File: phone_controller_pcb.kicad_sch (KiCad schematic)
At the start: 4 parts, among them U1 nRF52840, Y1 ECS-320-8-37B-CKY-TR, Y2 ABS05-32.768KHZ-9-T

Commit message: Added Usb esd protection
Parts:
- added J1: USB_C_Receptacle_USB2.0_14P, Connector_USB:USB_C_Receptacle_G-Switch_GT-USB-7010ASV, symbol Connector:USB_C_Receptacle_USB2.0_14P
- added U2: USBLC6-2P6, Package_TO_SOT_SMD:SOT-666, symbol Power_Protection:USBLC6-2P6
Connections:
- net GND: now also J1.A1 (GND), J1.A12 (GND), J1.B1 (GND), J1.B12 (GND), J1.S1 (SHIELD)
- net +5V: now reaches U1.AD2 (VBUS)
- net +5V: now also U1.Y2 (VDDH), J1.A4 (VBUS), J1.A9 (VBUS), J1.B4 (VBUS), J1.B9 (VBUS)
- net USB_D-: now reaches U1.AD4 (D-)
- net USB_D-: now also U2.6 (I/O1)
- net USB_D+: now reaches U1.AD6 (D+)
- net USB_D+: now also U2.4 (I/O2)
- new net: J1.A6 (D+), J1.B6 (D+), U2.3 (I/O2)
- new net: J1.A7 (D-), J1.B7 (D-), U2.1 (I/O1)
- new net CC1: J1.A5 (CC1)
- new net CC2: J1.B5 (CC2)
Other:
- moved on the sheet: AE1, U1, Y1, Y2

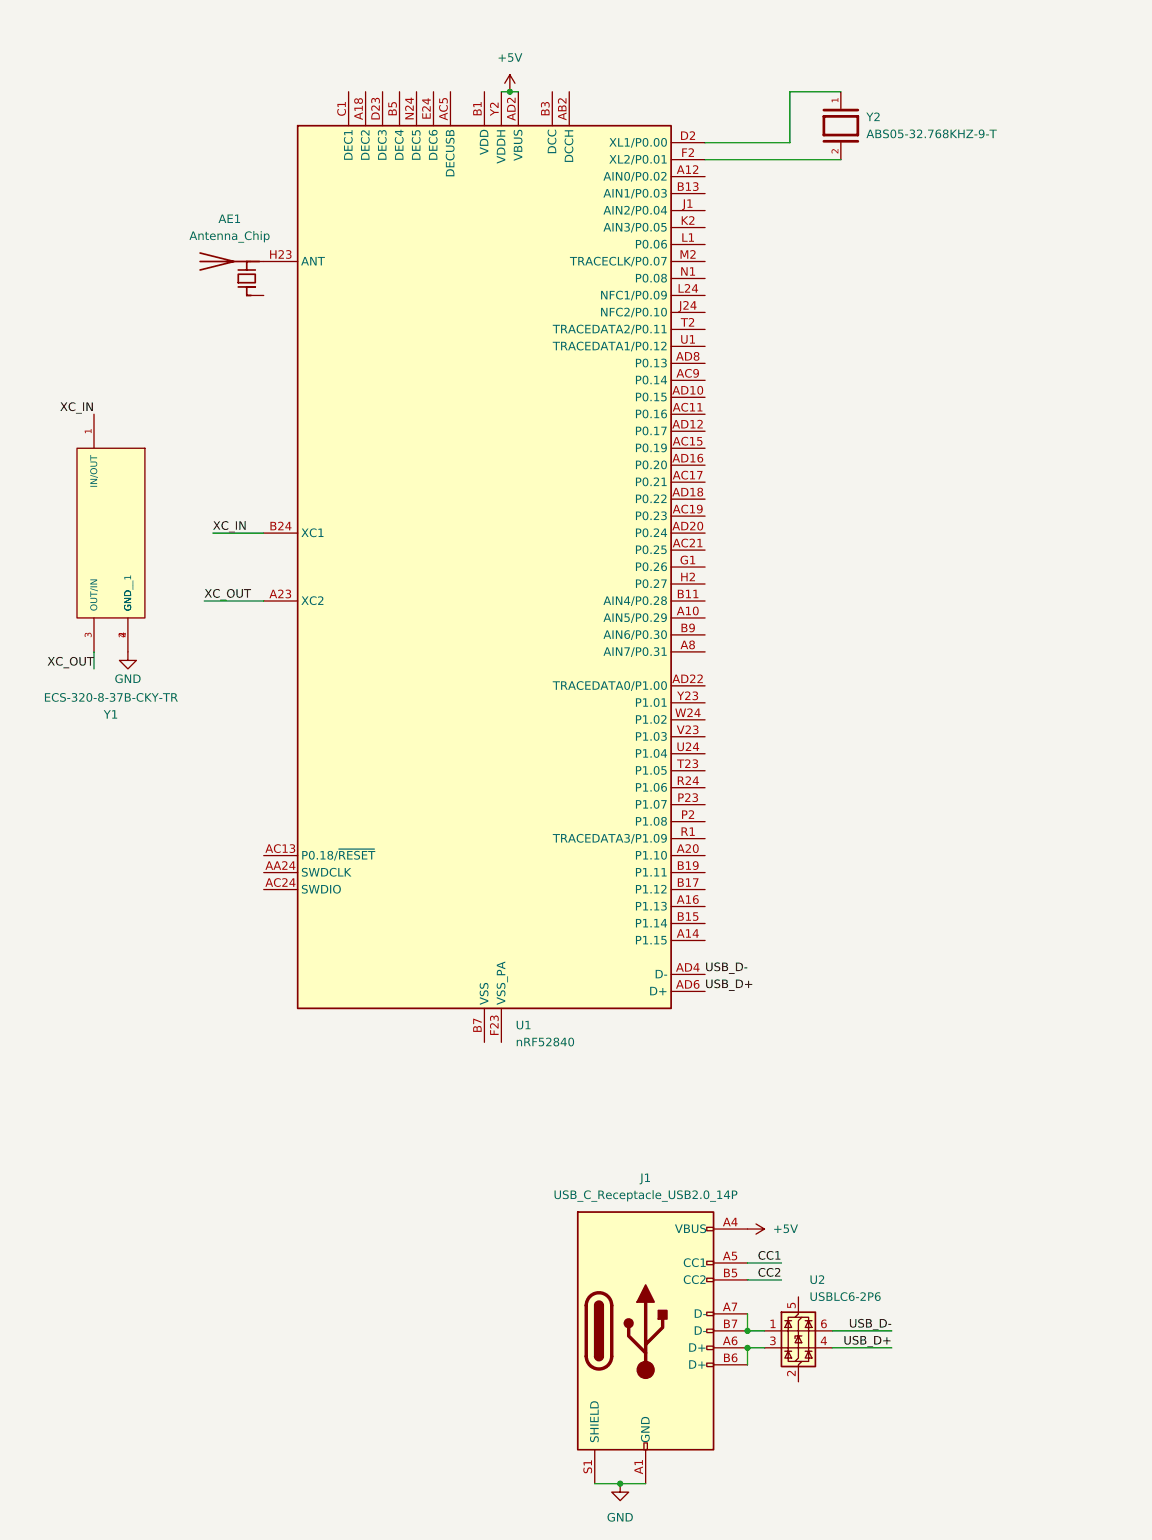
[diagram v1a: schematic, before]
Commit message: Added mcu digikey links and make sure footprint is correct; Added SWD pinouts for initial flash + debugger capability from nordic dk
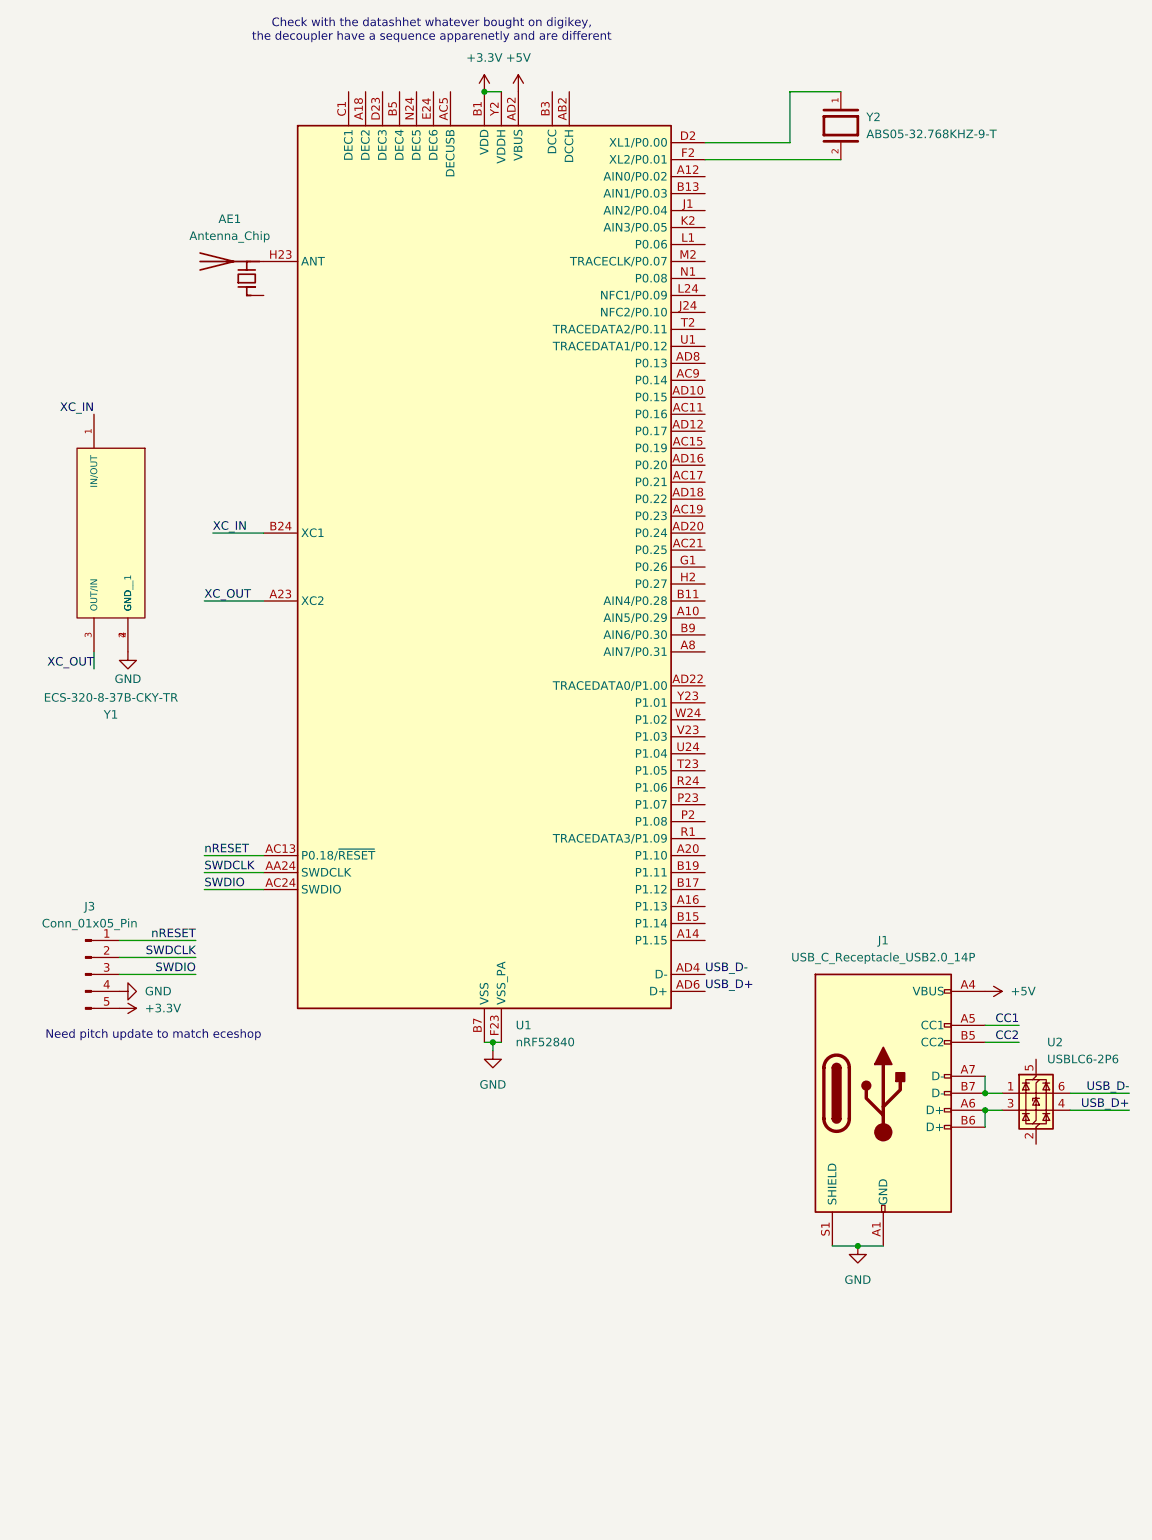
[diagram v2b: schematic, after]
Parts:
- added J3: Conn_01x05_Pin, Connector_PinHeader_1.00mm:PinHeader_1x05_P1.00mm_Vertical, symbol Connector:Conn_01x05_Pin
- U1: Digikey (none) -> https://www.digikey.com/en/products/detail/nordic-semicondu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
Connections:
- net +5V: no longer U1.Y2 (VDDH)
- net GND: now also U1.B7 (VSS), U1.EP (VSS), U1.F23 (VSS_PA), J3.4 (Pin_4)
- net +3.3V: now reaches U1.A22 (VDD), U1.AD14 (VDD), U1.AD23 (VDD), U1.B1 (VDD), U1.W1 (VDD)
- net +3.3V: now also U1.Y2 (VDDH), J3.5 (Pin_5)
- net SWDCLK: now reaches U1.AA24 (SWDCLK)
- net SWDCLK: now also J3.2 (Pin_2)
- net nRESET: now reaches U1.AC13 (P0.18/~{RESET})
- net nRESET: now also J3.1 (Pin_1)
- net SWDIO: now reaches U1.AC24 (SWDIO)
- net SWDIO: now also J3.3 (Pin_3)
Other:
- note added: "Check with the datashhet whatever bought on digikey, the decoupler have a sequence apparenetly and are different"
- note added: "Need pitch update to match eceshop"
- moved on the sheet: J1, U2

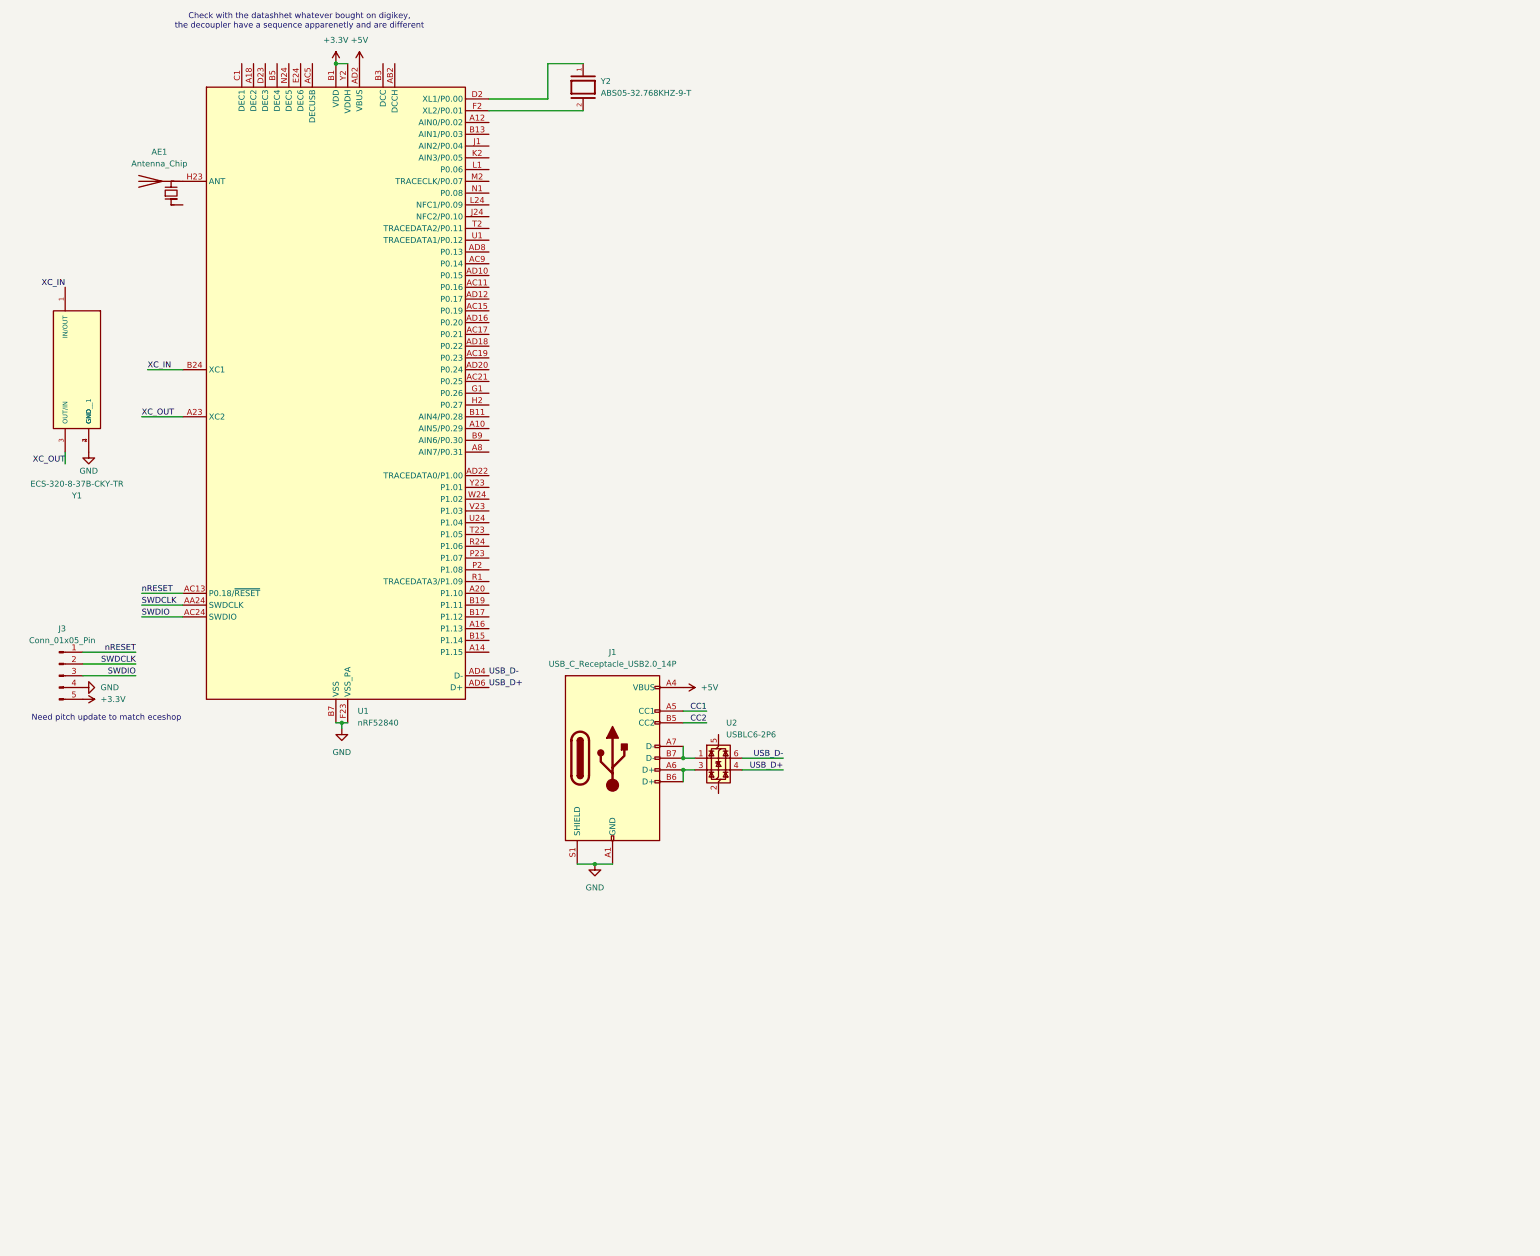
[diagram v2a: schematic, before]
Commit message: Added decoupling capacitor and setup for joycon pinouts
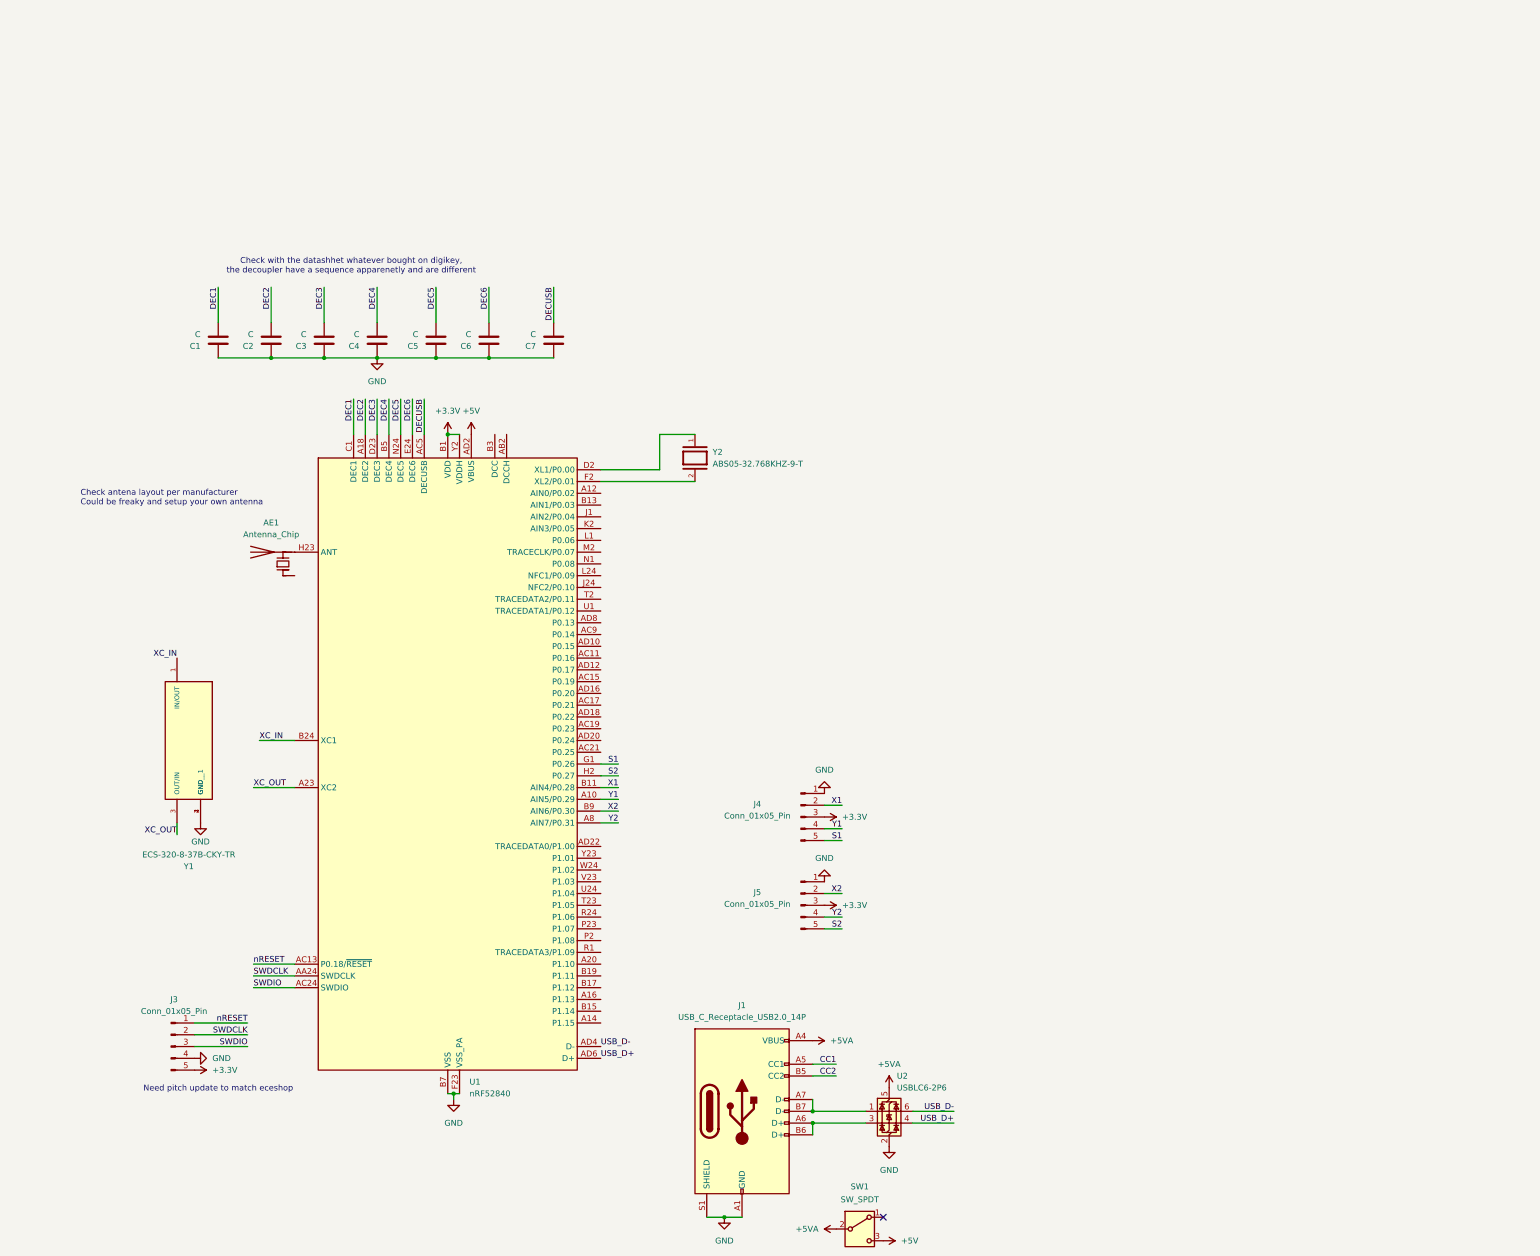
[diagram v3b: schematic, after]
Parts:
- added C1, C2, C3, C4, C5, C6, C7: C, Capacitor_SMD:C_0805_2012Metric, symbol Device:C
- added J4, J5: Conn_01x05_Pin, Connector_PinHeader_1.00mm:PinHeader_1x05_P1.00mm_Vertical, symbol Connector:Conn_01x05_Pin
- added SW1: SW_SPDT, symbol Switch:SW_SPDT
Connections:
- net +3.3V: now also J4.3 (Pin_3), J5.3 (Pin_3)
- net +5V: now also SW1.3 (C); no longer J1.A4 (VBUS), J1.A9 (VBUS), J1.B4 (VBUS), J1.B9 (VBUS)
- net GND: now also U2.2 (GND), C1.2, C2.2, C3.2, C4.2, C5.2, C6.2, C7.2, J4.1 (Pin_1), J5.1 (Pin_1)
- net +5VA: now reaches U2.5 (VBUS)
- net +5VA: now also J1.A4 (VBUS), J1.A9 (VBUS), J1.B4 (VBUS), J1.B9 (VBUS), SW1.2 (B)
- net Y1: now reaches U1.A10 (AIN5/P0.29)
- net Y1: now also J4.4 (Pin_4)
- net DEC2: now reaches U1.A18 (DEC2)
- net DEC2: now also C2.1
- net Y2: now reaches U1.A8 (AIN7/P0.31)
- net Y2: now also J5.4 (Pin_4)
- net DECUSB: now reaches U1.AC5 (DECUSB)
- net DECUSB: now also C7.1
- net X1: now reaches U1.B11 (AIN4/P0.28)
- net X1: now also J4.2 (Pin_2)
- net DEC4: now reaches U1.B5 (DEC4)
- net DEC4: now also C4.1
- net X2: now reaches U1.B9 (AIN6/P0.30)
- net X2: now also J5.2 (Pin_2)
- net DEC1: now reaches U1.C1 (DEC1)
- net DEC1: now also C1.1
- net DEC3: now reaches U1.D23 (DEC3)
- net DEC3: now also C3.1
- net DEC6: now reaches U1.E24 (DEC6)
- net DEC6: now also C6.1
- net S1: now reaches U1.G1 (P0.26)
- net S1: now also J4.5 (Pin_5)
- net S2: now reaches U1.H2 (P0.27)
- net S2: now also J5.5 (Pin_5)
- net DEC5: now reaches U1.N24 (DEC5)
- net DEC5: now also C5.1
- no-connect marks 0 -> 1
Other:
- note added: "Check antena layout per manufacturer Could be freaky and setup your own antenna"
- moved on the sheet: AE1, J1, J3, U1, U2, Y1, Y2
